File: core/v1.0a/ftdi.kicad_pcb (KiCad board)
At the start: 2 copper layers, 32 x 20 mm, 36 parts, among them J1 Conn, P1 pkl_USB_OTG, P2 UP, P3 UP, P4 UP, P5 UP, U1 93C46B-SOT-23-6, U2 FT232H, X1 12MHz

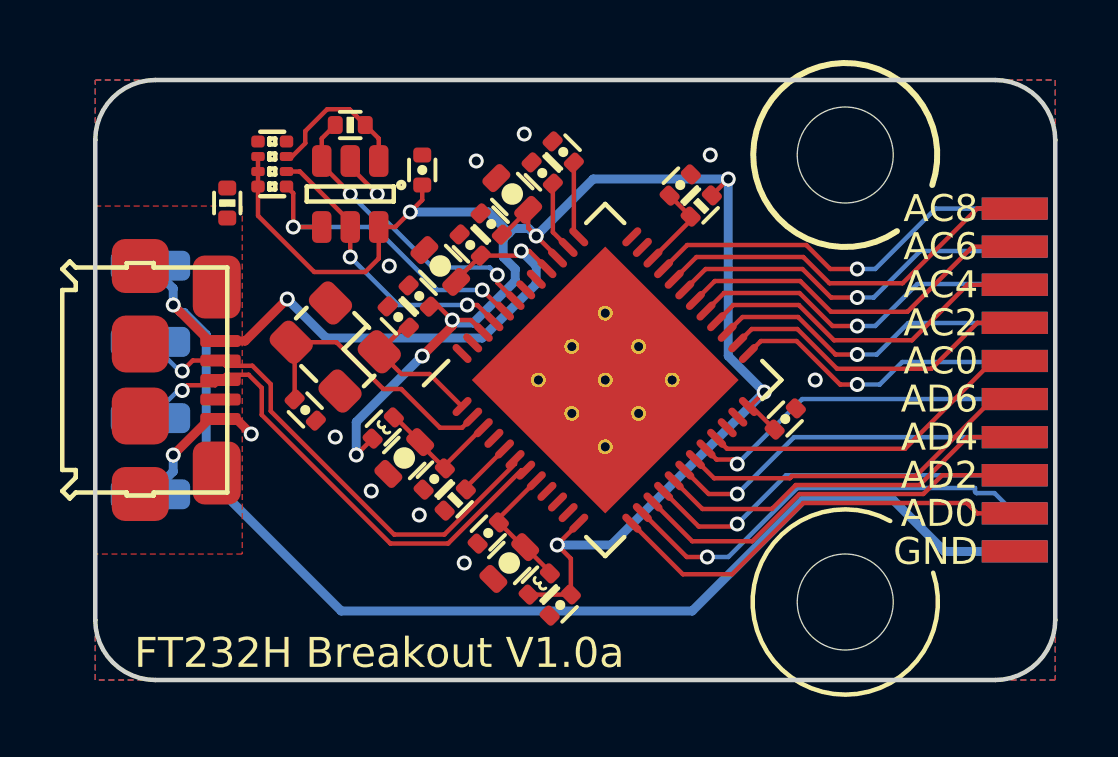
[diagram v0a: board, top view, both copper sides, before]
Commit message: Bumped the ftdi adapter to V1.0a. + minor improvements.
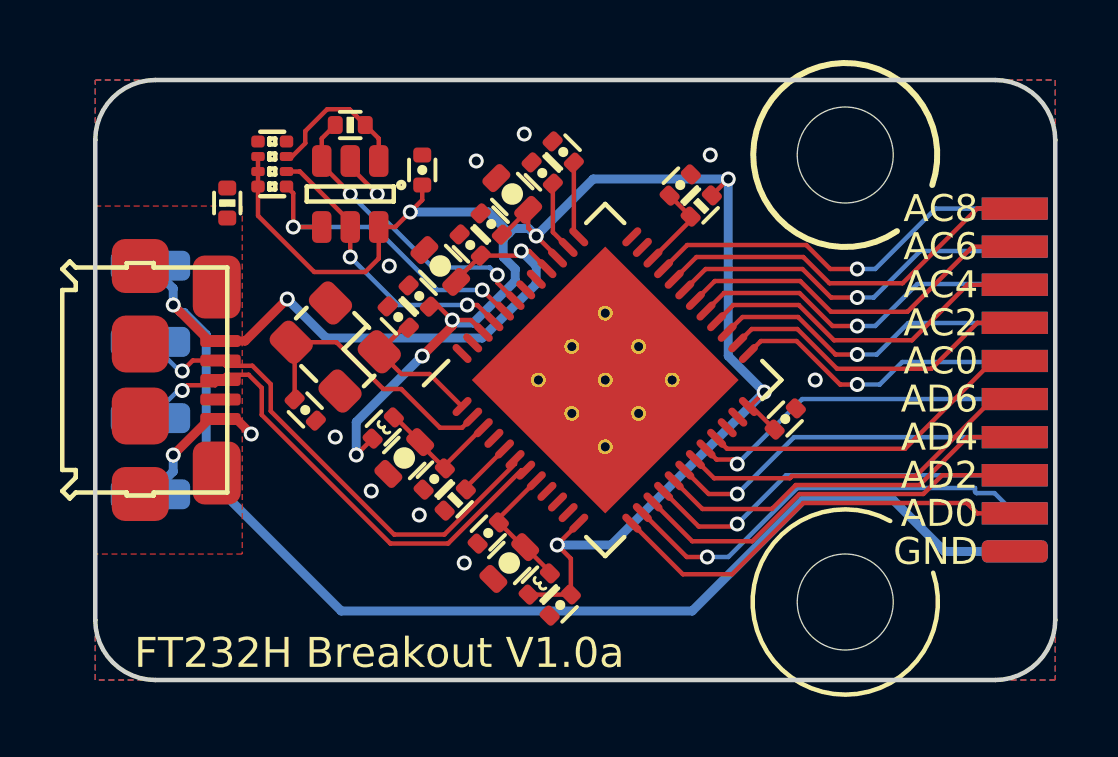
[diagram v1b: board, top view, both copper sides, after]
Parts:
- removed the REF** at (43.1, 47.5)
- J1: moved to F.Cu
- turned J1 to 90 degrees
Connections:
- J1 pad 1: /ACBUS9 -> GND
- J1 pad 10: /ACBUS0 -> /ADBUS7
- J1 pad 11: /ADBUS7 -> /ACBUS0
- J1 pad 12: /ADBUS6 -> /ACBUS1
- J1 pad 13: /ADBUS5 -> /ACBUS2
- J1 pad 14: /ADBUS4 -> /ACBUS3
- J1 pad 15: /ADBUS3 -> /ACBUS4
- J1 pad 16: /ADBUS2 -> /ACBUS5
- J1 pad 17: /ADBUS1 -> /ACBUS6
- J1 pad 18: /ADBUS0 -> /ACBUS7
- J1 pad 19: +5V -> /ACBUS8
- J1 pad 2: /ACBUS8 -> +5V
- J1 pad 20: GND -> /ACBUS9
- J1 pad 3: /ACBUS7 -> /ADBUS0
- J1 pad 4: /ACBUS6 -> /ADBUS1
- J1 pad 5: /ACBUS5 -> /ADBUS2
- J1 pad 6: /ACBUS4 -> /ADBUS3
- J1 pad 7: /ACBUS3 -> /ADBUS4
- J1 pad 8: /ACBUS2 -> /ADBUS5
- J1 pad 9: /ACBUS1 -> /ADBUS6
